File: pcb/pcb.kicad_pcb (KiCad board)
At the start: 2 copper layers, 60 x 45 mm, 18 parts

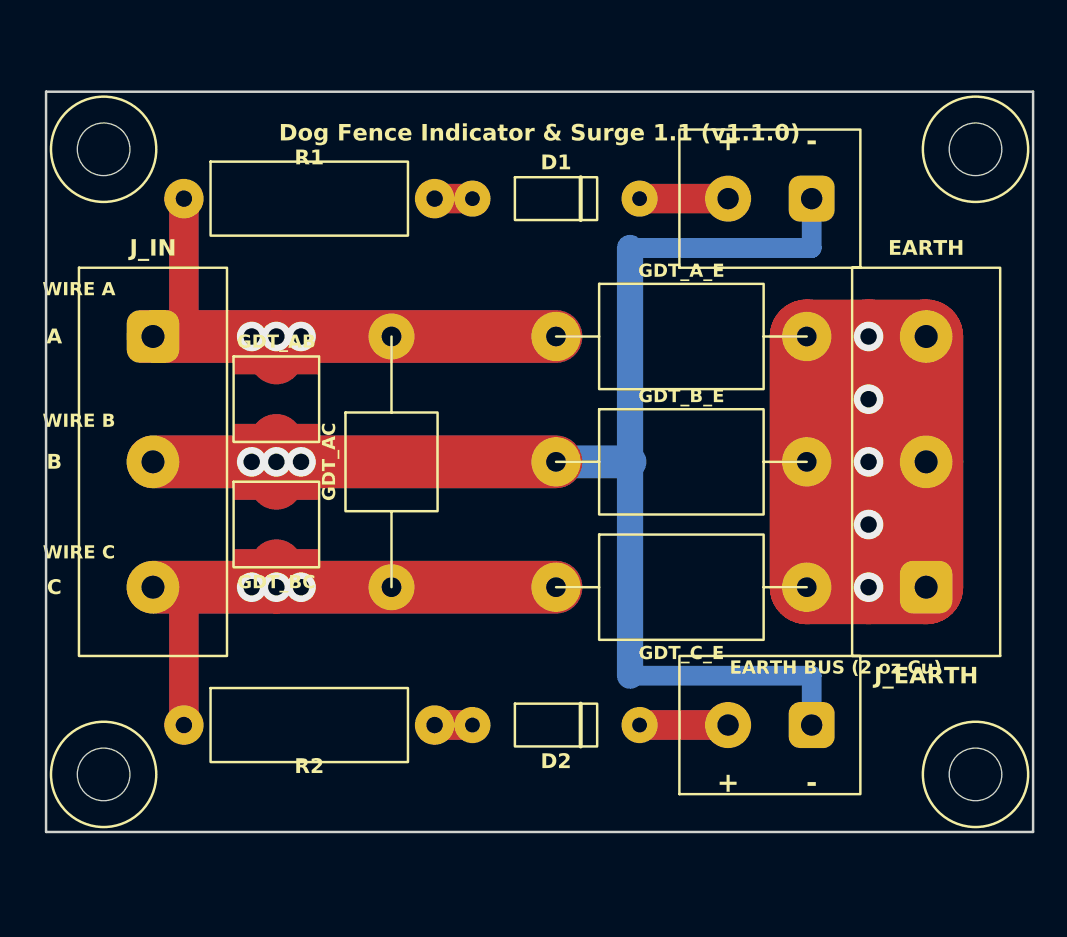
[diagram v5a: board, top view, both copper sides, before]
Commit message: Add courtyards for components that were clashing.
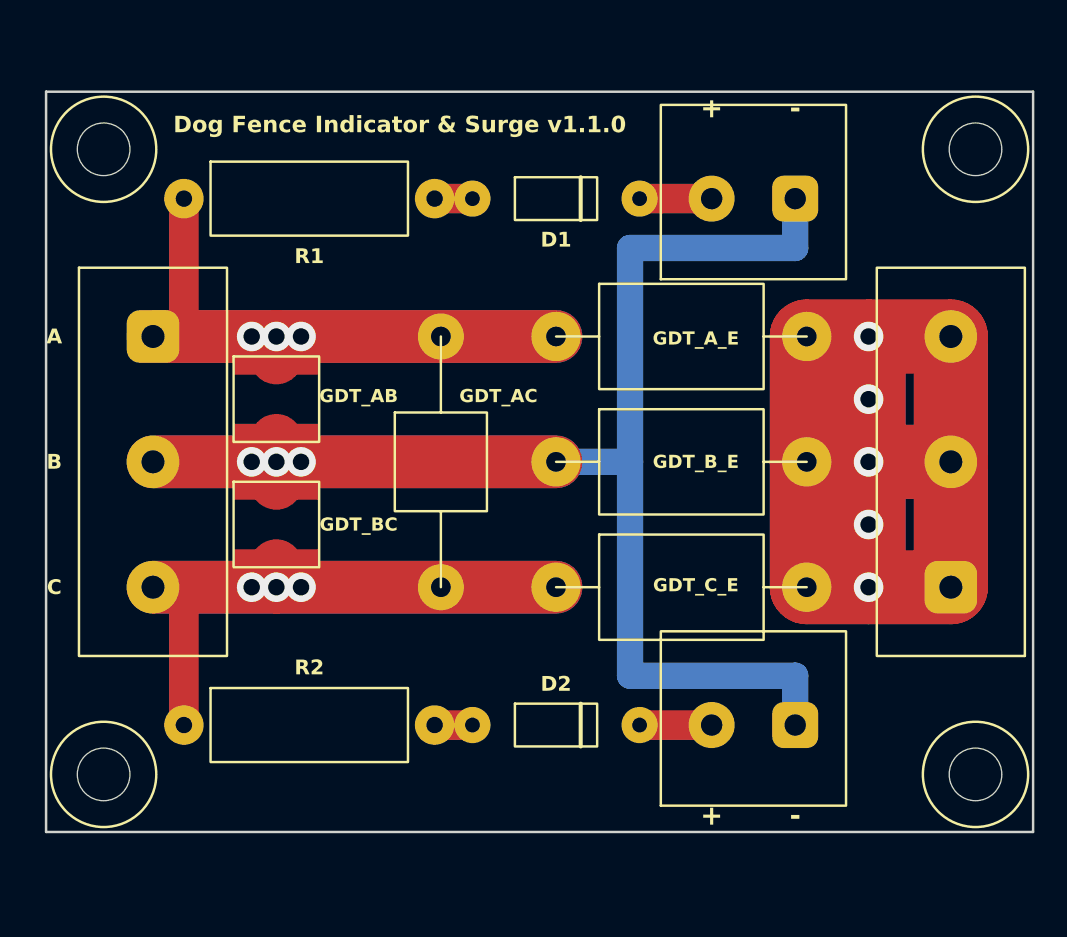
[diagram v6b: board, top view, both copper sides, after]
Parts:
- moved GDT_AC 3.00 mm to (124.0, 122.5)
- moved J_EARTH 1.50 mm to (155.0, 122.5)
- moved J_LED_A 1.00 mm to (143.0, 106.5)
- moved J_LED_C 1.00 mm to (143.0, 138.5)
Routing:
- net EARTH: track 135.0 -> 144.0 mm
- net WIRE_B: track 110.2 -> 108.2 mm
- net LED_C_POS: track 5.38 -> 4.38 mm
- net LED_A_POS: track 5.38 -> 4.38 mm
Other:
- board text added: "Dog Fence Indicator & Surge v1.1.0"
- board text removed: "Dog Fence Indicator & Surge 1.1 (v1.1.0)"
- board text removed: "EARTH BUS (2 oz Cu)"
- board text removed: "WIRE A"
- board text removed: "WIRE B"
- board text removed: "WIRE C"

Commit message: Widen the board for better clearances
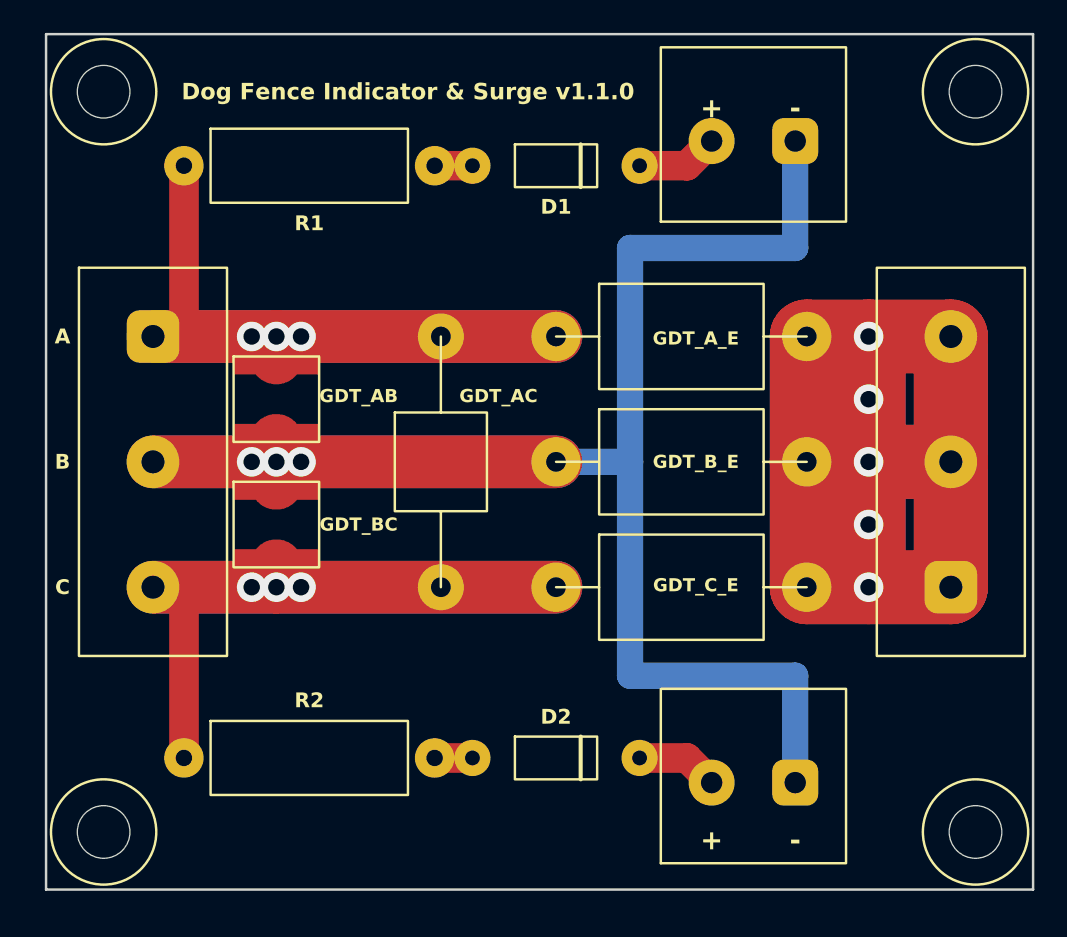
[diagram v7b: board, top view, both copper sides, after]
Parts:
- moved H1 3.50 mm to (103.5, 100.0)
- moved H2 3.50 mm to (156.5, 100.0)
- moved H3 3.50 mm to (103.5, 145.0)
- moved H4 3.50 mm to (156.5, 145.0)
- moved J_LED_A 3.50 mm to (143.0, 103.0)
- moved J_LED_C 3.50 mm to (143.0, 142.0)
- moved D1 2.00 mm to (131.0, 104.5)
- moved D2 2.00 mm to (131.0, 140.5)
- moved R1 2.00 mm to (116.0, 104.5)
- moved R2 2.00 mm to (116.0, 140.5)
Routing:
- net WIRE_B: track 108.2 -> 115.2 mm
- net WIRE_C: track 58.7 -> 60.7 mm
- net WIRE_A: track 58.7 -> 60.7 mm
- net LED_C_POS: track 4.38 -> 5.00 mm
- net LED_A_POS: track 4.38 -> 5.00 mm
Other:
- board size 60 x 45 mm -> 60 x 52 mm
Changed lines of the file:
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@@
 	(footprint "MountingHole:MountingHole_3.2mm_M3"
 		(layer "F.Cu")
-		(at 103.5 103.5)
+		(at 103.5 100)
 		(property "Reference" "H1"
 			(at 0 0 0)
@@
 	(footprint "MountingHole:MountingHole_3.2mm_M3"
 		(layer "F.Cu")
-		(at 156.5 103.5)
+		(at 156.5 100)
 		(property "Reference" "H2"
 			(at 0 0 0)
@@
 	(footprint "MountingHole:MountingHole_3.2mm_M3"
 		(layer "F.Cu")
-		(at 103.5 141.5)
+		(at 103.5 145)
 		(property "Reference" "H3"
 			(at 0 0 0)
@@
 	(footprint "MountingHole:MountingHole_3.2mm_M3"
 		(layer "F.Cu")
-		(at 156.5 141.5)
+		(at 156.5 145)
 		(property "Reference" "H4"
 			(at 0 0 0)
@@
 	(footprint "Diode_THT:D_DO-41_SOD81_P10.16mm_Horizontal"
 		(layer "F.Cu")
-		(at 131 106.5)
+		(at 131 104.5)
 		(property "Reference" "D1"
 			(at 0 2.5 0)
@@
 	(footprint "TerminalBlock_Phoenix:TerminalBlock_Phoenix_MKDS-1,5-2-5.08_1x02_P5.08mm_Horizontal"
 		(layer "F.Cu")
-		(at 143 106.5 90)
+		(at 143 103 90)
 		(property "Reference" "J_LED_A"
 			(at 0 0 0)
@@
 		)
 		(fp_text user "C"
-			(at -6 7.62 0)
+			(at -5.5 7.62 0)
 			(layer "F.SilkS")
 			(effects
@@
 		)
 		(fp_text user "A"
-			(at -6 -7.62 0)
+			(at -5.5 -7.62 0)
 			(layer "F.SilkS")
 			(effects
@@
 		)
 		(fp_text user "B"
-			(at -6 0 0)
+			(at -5.5 0 0)
 			(layer "F.SilkS")
 			(effects
@@
 	(footprint "Resistor_THT:R_Axial_DIN0414_L11.9mm_D4.5mm_P15.24mm_Horizontal"
 		(layer "F.Cu")
-		(at 116 138.5)
+		(at 116 140.5)
 		(property "Reference" "R2"
 			(at 0 -3.5 0)
@@
 	(footprint "Resistor_THT:R_Axial_DIN0414_L11.9mm_D4.5mm_P15.24mm_Horizontal"
 		(layer "F.Cu")
-		(at 116 106.5)
+		(at 116 104.5)
 		(property "Reference" "R1"
 			(at 0 3.5 0)
@@
 	(footprint "TerminalBlock_Phoenix:TerminalBlock_Phoenix_MKDS-1,5-2-5.08_1x02_P5.08mm_Horizontal"
 		(layer "F.Cu")
-		(at 143 138.5 90)
+		(at 143 142 90)
 		(property "Reference" "J_LED_C"
 			(at 0 0 0)
@@
 	(footprint "Diode_THT:D_DO-41_SOD81_P10.16mm_Horizontal"
 		(layer "F.Cu")
-		(at 131 138.5)
+		(at 131 140.5)
 		(property "Reference" "D2"
 			(at 0 -2.5 0)
@@
 	)
 	(gr_rect
-		(start 100 100)
-		(end 160 145)
+		(start 100 96.5)
+		(end 160 148.5)
 		(stroke
 			(width 0.15)
@@
 	)
 	(gr_text "-"
-		(at 145.54 144 0)
+		(at 145.54 145.5 0)
 		(layer "F.SilkS")
 		(effects
@@
 	)
 	(gr_text "+"
-		(at 140.46 144 0)
+		(at 140.46 145.5 0)
 		(layer "F.SilkS")
 		(effects
@@
 	)
 	(gr_text "Dog Fence Indicator & Surge v1.1.0"
-		(at 121.5 102 0)
+		(at 122 100 0)
 		(layer "F.SilkS")
 		(effects
@@
 	(segment
 		(start 108.38 114.88)
-		(end 108.38 106.5)
+		(end 108.38 104.5)
 		(width 1.8)
 		(layer "F.Cu")
@@
 	(segment
 		(start 145.54 135.5)
-		(end 145.54 138.5)
+		(end 145.54 142)
 		(width 1.6)
 		(layer "B.Cu")
@@
 	(segment
 		(start 145.54 109.5)
-		(end 145.54 106.5)
+		(end 145.54 103)
 		(width 1.6)
 		(layer "B.Cu")
@@
 	(segment
 		(start 108.38 130.12)
-		(end 108.38 138.5)
+		(end 108.38 140.5)
 		(width 1.8)
 		(layer "F.Cu")
@@
 	)
 	(segment
-		(start 123.62 106.5)
-		(end 125.92 106.5)
+		(start 123.62 104.5)
+		(end 125.92 104.5)
 		(width 1.8)
 		(layer "F.Cu")
@@
 	)
 	(segment
-		(start 136.08 106.5)
-		(end 140.46 106.5)
+		(start 136.08 104.5)
+		(end 138.96 104.5)
 		(width 1.8)
 		(layer "F.Cu")
@@
 	)
 	(segment
-		(start 123.62 138.5)
-		(end 125.92 138.5)
+		(start 138.96 104.5)
+		(end 140.46 103)
 		(width 1.8)
 		(layer "F.Cu")
+		(net 6)
+	)
+	(segment
+		(start 123.62 140.5)
+		(end 125.92 140.5)
+		(width 1.8)
+		(layer "F.Cu")
 		(net 7)
 	)
 	(segment
-		(start 136.08 138.5)
-		(end 140.46 138.5)
+		(start 136.08 140.5)
+		(end 138.96 140.5)
 		(width 1.8)
 		(layer "F.Cu")
+		(net 8)
+	)
+	(segment
+		(start 138.96 140.5)
+		(end 140.46 142)
+		(width 1.8)
+		(layer "F.Cu")

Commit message: Clean up font usage
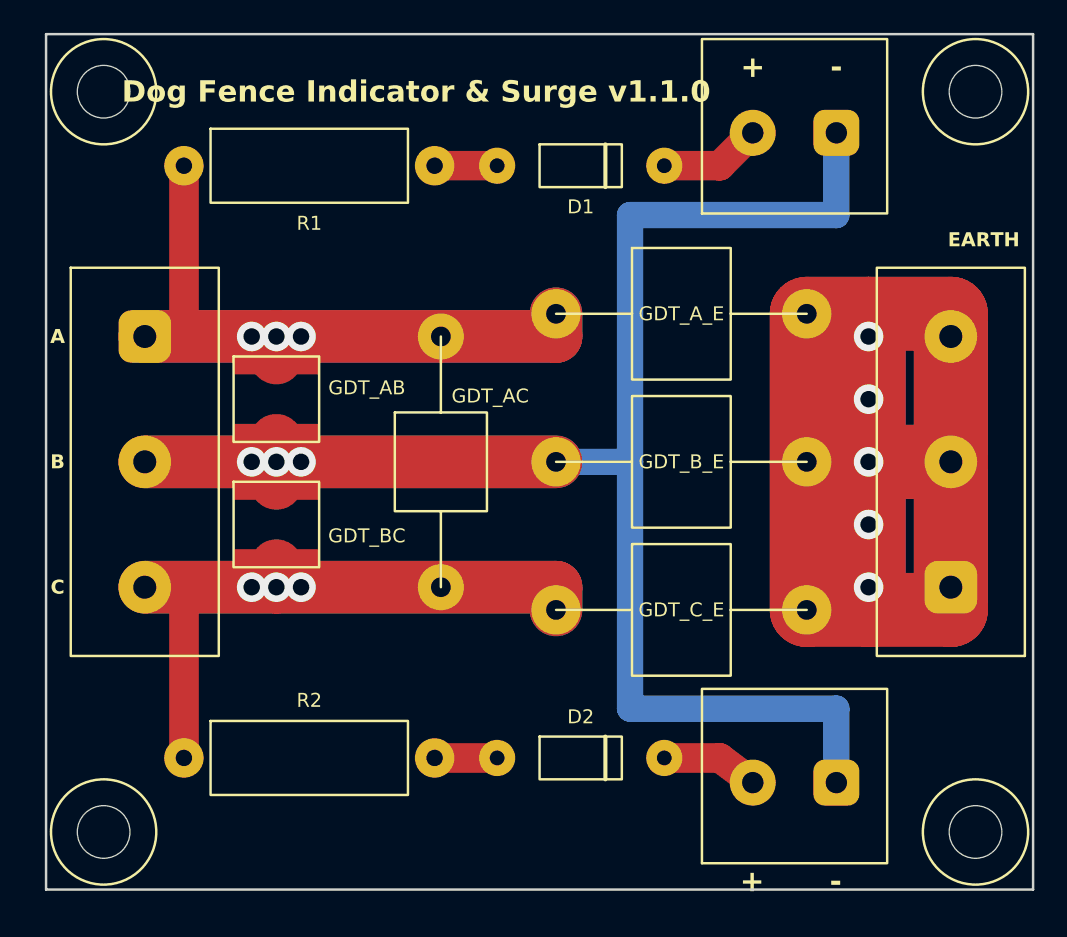
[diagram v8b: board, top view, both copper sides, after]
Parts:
- moved J_LED_A 2.55 mm to (145.5, 102.5)
- moved J_LED_C 2.50 mm to (145.5, 142.0)
- moved D1 1.50 mm to (132.5, 104.5)
- moved D2 1.50 mm to (132.5, 140.5)
- moved GDT_A_E 1.38 mm to (138.6, 113.5)
- moved GDT_C_E 1.38 mm to (138.6, 131.5)
- moved J_IN 0.50 mm to (106.0, 122.5)
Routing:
- net EARTH: track 144.0 -> 160.6 mm
- net WIRE_B: track 115.2 -> 121.7 mm
- net WIRE_C: track 60.7 -> 64.4 mm
- net WIRE_A: track 60.7 -> 64.4 mm
- net Net-(D2-A): track 2.30 -> 3.80 mm
- net Net-(D1-A): track 2.30 -> 3.80 mm
- net LED_A_POS: track 5.00 -> 6.21 mm
- net LED_C_POS: track 5.00 -> 5.88 mm
